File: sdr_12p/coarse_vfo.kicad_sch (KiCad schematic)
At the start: 1 part, among them U8 ADF4351

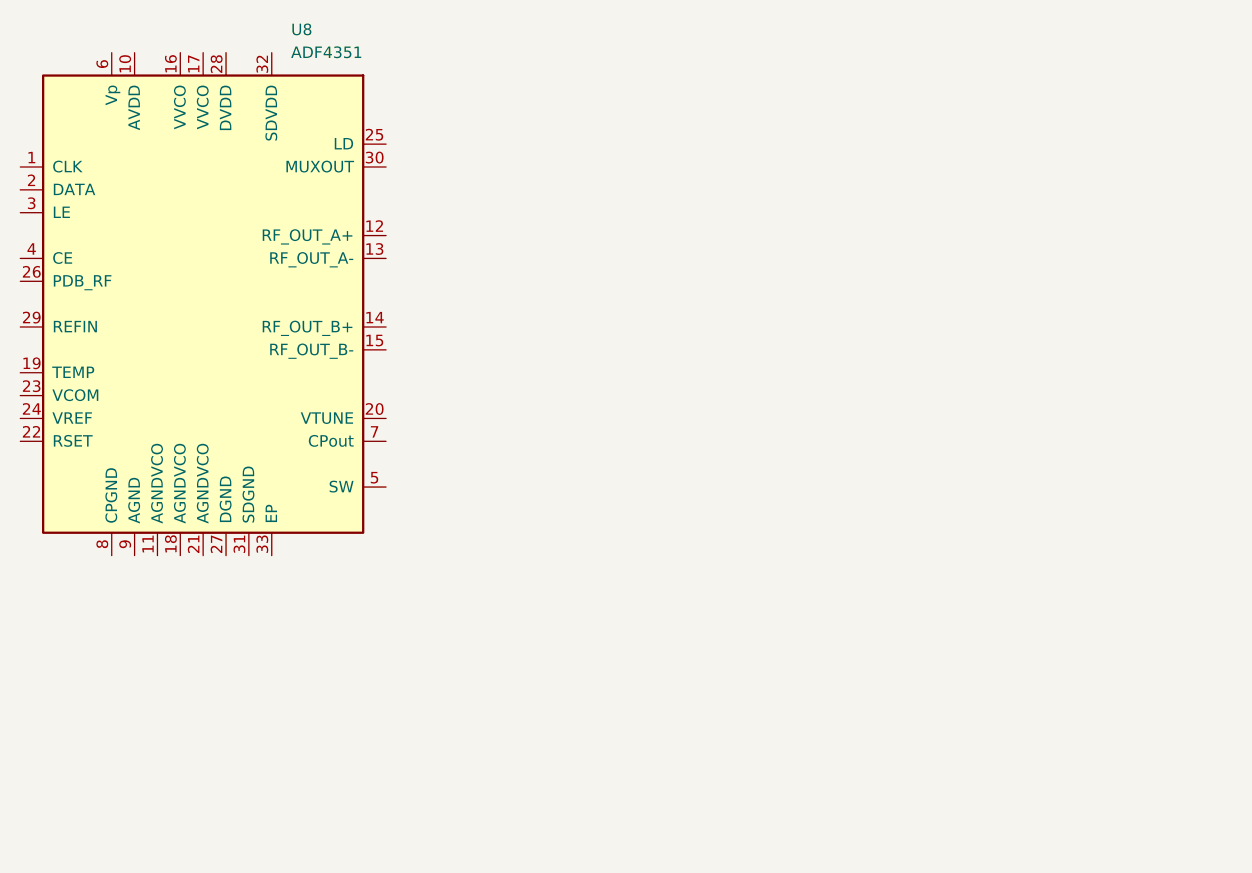
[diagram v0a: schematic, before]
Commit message: added uC
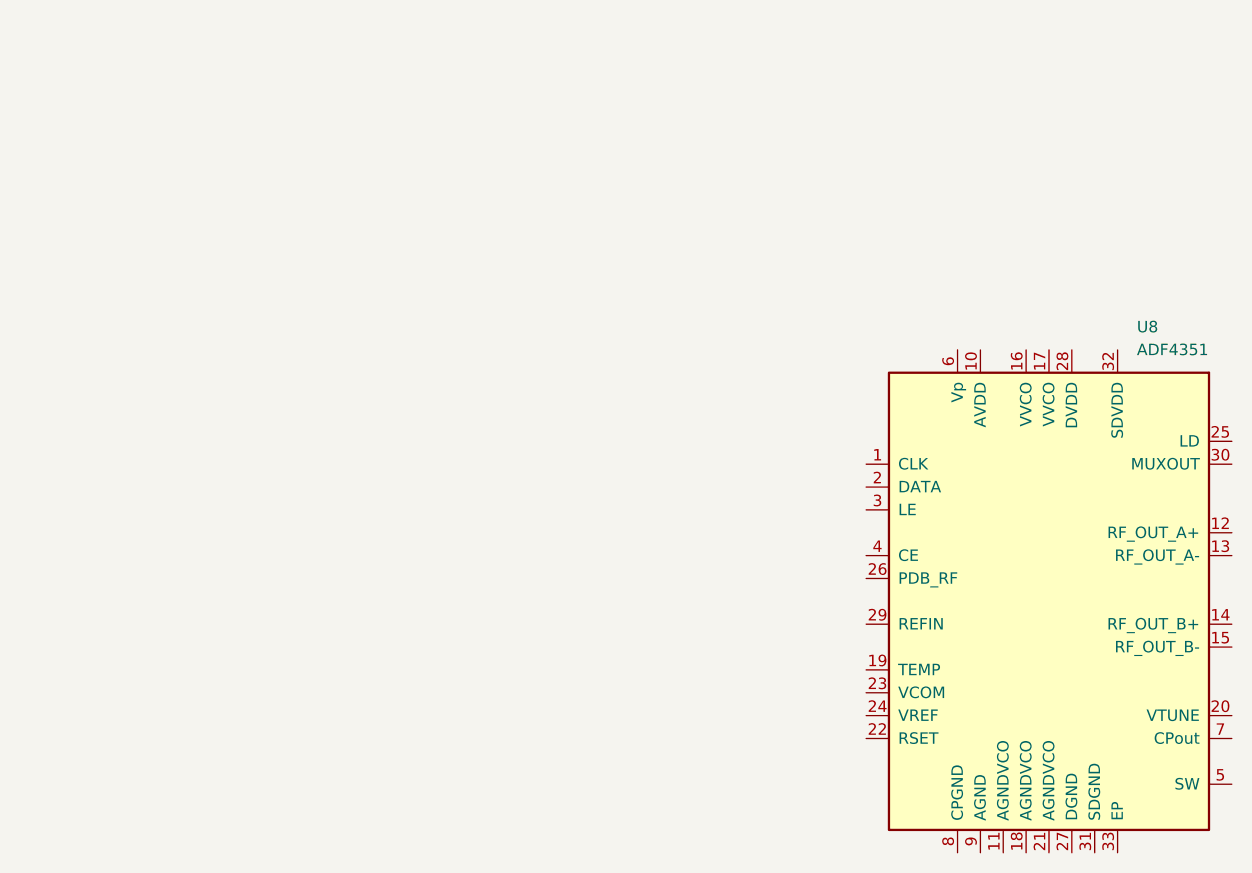
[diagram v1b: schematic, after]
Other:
- company: (none) -> Andy McCann KA3KAF and Doug McCann KA3KAG
- title: (none) -> Coarse VFO
- moved on the sheet: U8
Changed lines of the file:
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@@
 	(generator "eeschema")
 	(generator_version "9.0")
-	(paper "A4")
+	(paper "B")
+	(title_block
+		(title "Coarse VFO")
+		(date "2026-01-02")
+		(rev "0.0")
+		(company "Andy McCann KA3KAF and Doug McCann KA3KAG")
+	)
 	(symbol
 		(lib_id "Timer_PLL:ADF4351")
-		(at 134.62 90.17 0)
+		(at 228.6 123.19 0)
 		(unit 1)
 		(exclude_from_sim no)
@@
 		(fields_autoplaced yes)
 		(property "Reference" "U8"
-			(at 144.3833 59.69 0)
+			(at 238.3633 92.71 0)
 			(effects
 				(font
@@
 		)
 		(property "Value" "ADF4351"
-			(at 144.3833 62.23 0)
+			(at 238.3633 95.25 0)
 			(effects
 				(font
@@
 		)
 		(property "Footprint" "Package_CSP:LFCSP-32-1EP_5x5mm_P0.5mm_EP3.25x3.25mm"
-			(at 134.62 90.17 0)
+			(at 228.6 123.19 0)
 			(effects
 				(font
@@
 		)
 		(property "Datasheet" "https://www.analog.com/media/en/technical-documentation/data-sheets/ADF4351.pdf"
-			(at 134.62 90.17 0)
+			(at 228.6 123.19 0)
 			(effects
 				(font
@@
 		)
 		(property "Description" "35-4400MHz fractional-N PLL, LFCSP-32"
-			(at 134.62 90.17 0)
+			(at 228.6 123.19 0)
 			(effects
 				(font
@@
 		)
 		(instances
+			(project "coarse_vfo"
+				(path "/afb03079-dce4-49ba-80a9-794cb150e1fe"
+					(reference "U?")
+					(unit 1)
+				)
+			)
 			(project "sdr_12p"
 				(path "/fe42ca2f-2bb8-4d5a-9e84-807788ed632f/8e9b59d6-8c0d-4684-98b0-c19302bc7c8e"
@@
 		)
 	)
+	(sheet_instances
+		(path "/"
+			(page "1")
+		)
+	)
+	(embedded_fonts no)
 )
